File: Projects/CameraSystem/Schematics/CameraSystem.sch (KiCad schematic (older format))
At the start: 1 part, among them J1 USB_B_MICRO_SMD

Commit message: feat: set up layout
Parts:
- removed J1: USB_B_MICRO_SMD, MyLibraries:USB_B_MICRO_SMD, symbol USB_B_MICRO_SMD
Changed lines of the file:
@@
 EESchema Schematic File Version 2
+LIBS:cl-connectors
+LIBS:dk_Addressable-Specialty
+LIBS:dk_Alarms-Buzzers-and-Sirens
+LIBS:dk_Automotive-Relays
+LIBS:dk_Balun
+LIBS:dk_Barrel-Audio-Connectors
+LIBS:dk_Battery-Holders-Clips-Contacts
+LIBS:dk_Clock-Timing-Clock-Generators-PLLs-Frequency-Synthesizers
+LIBS:dk_Clock-Timing-Programmable-Timers-and-Oscillators
+LIBS:dk_Clock-Timing-Real-Time-Clocks
+LIBS:dk_Coaxial-Connectors-RF
+LIBS:dk_Current-Transducers
+LIBS:dk_Data-Acquisition-ADCs-DACs-Special-Purpose
+LIBS:dk_Data-Acquisition-Analog-to-Digital-Converters-ADC
+LIBS:dk_Data-Acquisition-Digital-Potentiometers
+LIBS:dk_Data-Acquisition-Digital-to-Analog-Converters-DAC
+LIBS:dk_Data-Acquisition-Touch-Screen-Controllers
+LIBS:dk_DC-DC-Converters
+LIBS:dk_Digital-Isolators
+LIBS:dk_Diodes-Bridge-Rectifiers
+LIBS:dk_Diodes-Rectifiers-Arrays
+LIBS:dk_Diodes-Rectifiers-Single
+LIBS:dk_Diodes-Zener-Single
+LIBS:dk_Display-Modules-LCD-OLED-Graphic
+LIBS:dk_Display-Modules-LED-Character-and-Numeric
+LIBS:dk_D-Sub-Connectors
+LIBS:dk_Embedded-Microcontrollers
+LIBS:dk_Encoders
+LIBS:dk_Evaluation-Boards-Sensors
+LIBS:dk_Ferrite-Beads-and-Chips
+LIBS:dk_Fixed-Inductors
+LIBS:dk_Fuses
+LIBS:dk_Gas-Sensors
+LIBS:dk_Humidity-Moisture-Sensors
+LIBS:dk_Image-Sensors-Camera
+LIBS:dk_Infrared-UV-Visible-Emitters
+LIBS:dk_Inrush-Current-Limiters-ICL
+LIBS:dk_Interface-Analog-Switches-Multiplexers-Demultiplexers
+LIBS:dk_Interface-Analog-Switches-Special-Purpose
+LIBS:dk_Interface-Controllers
+LIBS:dk_Interface-Drivers-Receivers-Transceivers
+LIBS:dk_Interface-I-O-Expanders
+LIBS:dk_Interface-Modules
+LIBS:dk_Interface-Sensor-and-Detector-Interfaces
+LIBS:dk_Interface-Sensor-Capacitive-Touch
+LIBS:dk_Interface-Specialized
+LIBS:dk_LED-Indication-Discrete
+LIBS:dk_LEDs-Circuit-Board-Indicators-Arrays-Light-Bars-Bar-Graphs
+LIBS:dk_Linear-Amplifiers-Audio
+LIBS:dk_Linear-Amplifiers-Instrumentation-OP-Amps-Buffer-Amps
+LIBS:dk_Linear-Comparators
+LIBS:dk_Logic-Buffers-Drivers-Receivers-Transceivers
+LIBS:dk_Logic-Flip-Flops
+LIBS:dk_Logic-Gates-and-Inverters
+LIBS:dk_Logic-Multivibrators
+LIBS:dk_Logic-Shift-Registers
+LIBS:dk_Logic-Signal-Switches-Multiplexers-Decoders
+LIBS:dk_Logic-Translators-Level-Shifters
+LIBS:dk_Magnetic-Sensors-Compass-Magnetic-Field-Modules
+LIBS:dk_Magnetic-Sensors-Linear-Compass-ICs
+LIBS:dk_Magnetic-Sensors-Switches-Solid-State
+LIBS:dk_Memory
+LIBS:dk_Memory-Connectors-PC-Card-Sockets
+LIBS:dk_Microphones
+LIBS:dk_Modular-Connectors-Jacks
+LIBS:dk_Modular-Connectors-Jacks-With-Magnetics
+LIBS:dk_Motion-Sensors-Accelerometers
+LIBS:dk_Motion-Sensors-IMUs-Inertial-Measurement-Units
+LIBS:dk_Motion-Sensors-Tilt-Switches
+LIBS:dk_Navigation-Switches-Joystick
+LIBS:dk_Optical-Sensors-Ambient-Light-IR-UV-Sensors
+LIBS:dk_Optical-Sensors-Photo-Detectors-Remote-Receiver
+LIBS:dk_Optical-Sensors-Photodiodes
+LIBS:dk_Optical-Sensors-Phototransistors
+LIBS:dk_Optical-Sensors-Reflective-Analog-Output
+LIBS:dk_Optoisolators-Logic-Output
+LIBS:dk_Optoisolators-Transistor-Photovoltaic-Output
+LIBS:dk_Optoisolators-Triac-SCR-Output
+LIBS:dk_Oscillators
+LIBS:dk_PMIC-AC-DC-Converters-Offline-Switchers
+LIBS:dk_PMIC-Battery-Chargers
+LIBS:dk_PMIC-Battery-Management
+LIBS:dk_PMIC-Current-Regulation-Management
+LIBS:dk_PMIC-Full-Half-Bridge-Drivers
+LIBS:dk_PMIC-Gate-Drivers
+LIBS:dk_PMIC-LED-Drivers
+LIBS:dk_PMIC-Motor-Drivers-Controllers
+LIBS:dk_PMIC-OR-Controllers-Ideal-Diodes
+LIBS:dk_PMIC-Power-Distribution-Switches-Load-Drivers
+LIBS:dk_PMIC-Power-Management-Specialized
+LIBS:dk_PMIC-RMS-to-DC-Converters
+LIBS:dk_PMIC-Supervisors
+LIBS:dk_PMIC-Thermal-Management
+LIBS:dk_PMIC-V-F-and-F-V-Converters
+LIBS:dk_PMIC-Voltage-Reference
+LIBS:dk_PMIC-Voltage-Regulators-DC-DC-Switching-Controllers
+LIBS:dk_PMIC-Voltage-Regulators-DC-DC-Switching-Regulators
+LIBS:dk_PMIC-Voltage-Regulators-Linear
+LIBS:dk_PMIC-Voltage-Regulators-Special-Purpose
+LIBS:dk_Power-Relays-Over-2-Amps
+LIBS:dk_Pressure-Sensors-Transducers
+LIBS:dk_Programmable-Oscillators
+LIBS:dk_Pushbutton-Switches
+LIBS:dk_Rectangular-Connectors-Headers-Male-Pins
+LIBS:dk_Reed-Relays
+LIBS:dk_Resistor-Networks-Arrays
+LIBS:dk_RF-Amplifiers
+LIBS:dk_RF-Antennas
+LIBS:dk_RF-Demodulators
+LIBS:dk_RF-Detectors
+LIBS:dk_RF-Evaluation-and-Development-Kits-Boards
+LIBS:dk_RFID-RF-Access-Monitoring-ICs
+LIBS:dk_RF-Receivers
+LIBS:dk_RF-Switches
+LIBS:dk_RF-Transceiver-ICs
+LIBS:dk_RF-Transceiver-Modules
+LIBS:dk_RF-Transmitters
+LIBS:dk_Rotary-Potentiometers-Rheostats
+LIBS:dk_Sensors-Transducers_Accessories
+LIBS:dk_Signal-Relays-Up-to-2-Amps
+LIBS:dk_Slide-Switches
+LIBS:dk_Solid-State-Relays
+LIBS:dk_Specialized-ICs
+LIBS:dk_Specialized-Sensors
+LIBS:dk_Surge-Suppression-ICs
+LIBS:dk_Tactile-Switches
+LIBS:dk_Temperature-Sensors-Analog-and-Digital-Output
+LIBS:dk_Thermal-Cutoffs-Thermal-Fuses
+LIBS:dk_Thyristors-DIACs-SIDACs
+LIBS:dk_Thyristors-SCRs
+LIBS:dk_Thyristors-TRIACs
+LIBS:dk_Toggle-Switches
+LIBS:dk_Transistors-Bipolar-BJT-Arrays
+LIBS:dk_Transistors-Bipolar-BJT-RF
+LIBS:dk_Transistors-Bipolar-BJT-Single
+LIBS:dk_Transistors-Bipolar-BJT-Single-Pre-Biased
+LIBS:dk_Transistors-FETs-MOSFETs-Arrays
+LIBS:dk_Transistors-FETs-MOSFETs-RF
+LIBS:dk_Transistors-FETs-MOSFETs-Single
+LIBS:dk_Transistors-JFETs
+LIBS:dk_Trimmer-Potentiometers
+LIBS:dk_TVS-Diodes
+LIBS:dk_TVS-Mixed-Technology
+LIBS:dk_USB-DVI-HDMI-Connectors
 LIBS:power
 LIBS:device
@@
 LIBS:contrib
 LIBS:valves
-LIBS:cl-connectors
+LIBS:cl-integrated_circuits
+LIBS:CameraSystem-cache
 EELAYER 25 0
 EELAYER END
 $Descr A4 11693 8268
 encoding utf-8
-Sheet 1 1
+Sheet 1 6
 Title ""
 Date ""
@@
 Comment4 ""
 $EndDescr
-$Comp
-L USB_B_MICRO_SMD J1
-U 1 1 5BB11F8A
-P 1250 1750
-F 0 "J1" H 1250 1450 60  0000 C CNN
-F 1 "USB_B_MICRO_SMD" H 1250 2100 60  0000 C CNN
-F 2 "MyLibraries:USB_B_MICRO_SMD" H 1250 1750 60  0001 C CNN
-F 3 "" H 1250 1750 60  0001 C CNN
-	1    1250 1750
-	-1   0    0    -1
-$EndComp
+$Sheet
+S 1000 1000 900  650
+U 5BB4C1AE
+F0 "Input_Interface" 60
+F1 "Input_Interface.sch" 60
+F2 "VDD_5V0" O R 1900 1150 60
+F3 "D-" B R 1900 1300 60
+F4 "D+" B R 1900 1450 60
+$EndSheet
+$Sheet
+S 2700 1700 1100 1050
+U 5BB4D99F
+F0 "Microcontroller" 60
+F1 "Microcontroller.sch" 60
+$EndSheet
+$Sheet
+S 4700 900  1100 750
+U 5BB4D9C1
+F0 "Wifi" 60
+F1 "Wifi.sch" 60
+$EndSheet
+$Sheet
+S 4650 2100 1000 800
+U 5BB4DA56
+F0 "Memory" 60
+F1 "Memory.sch" 60
+$EndSheet
+$Sheet
+S 6200 2150 850  800
+U 5BB4DA63
+F0 "Camera" 60
+F1 "Camera.sch" 60
+$EndSheet
 $EndSCHEMATC

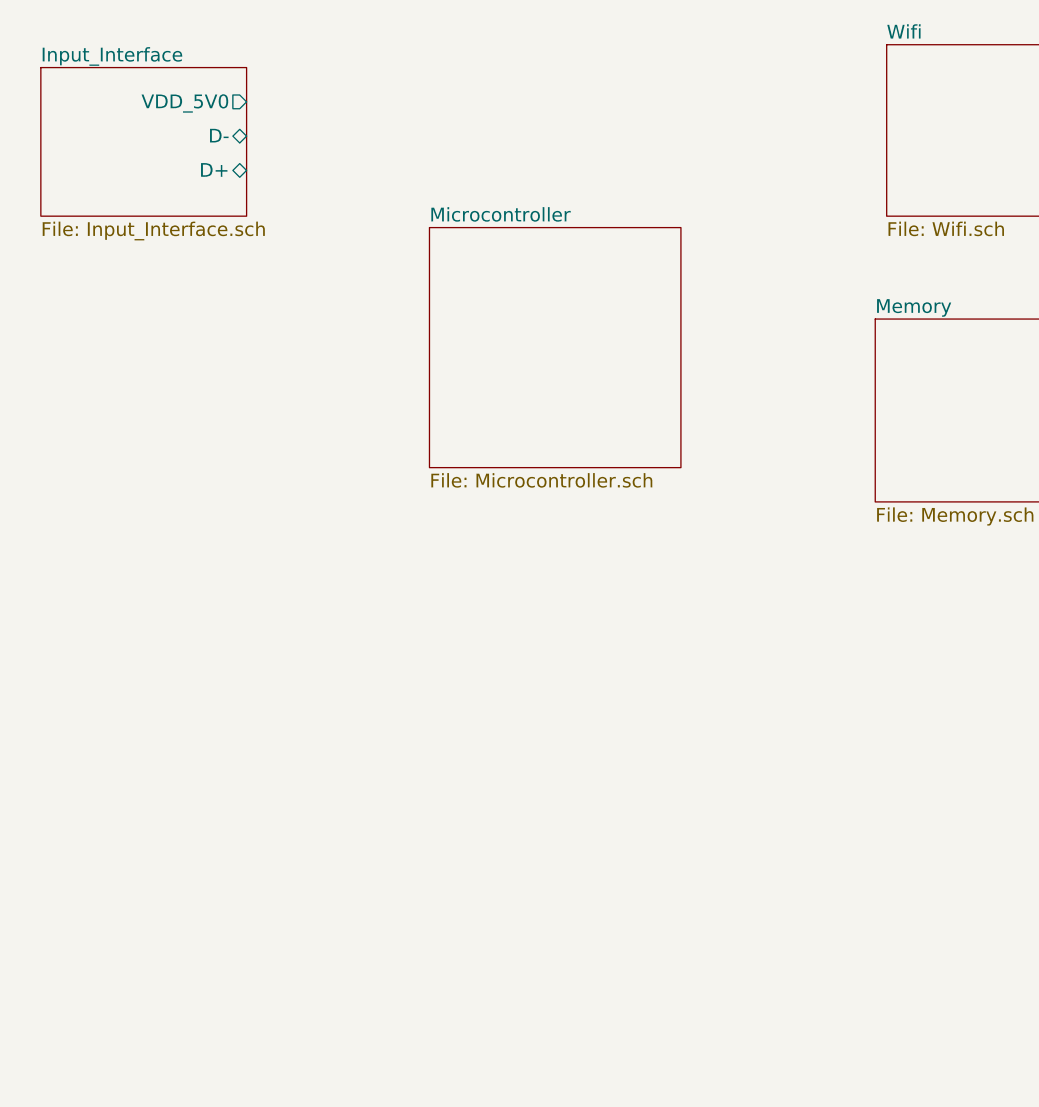
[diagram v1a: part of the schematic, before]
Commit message: feat:add led datasheets and microcontroler
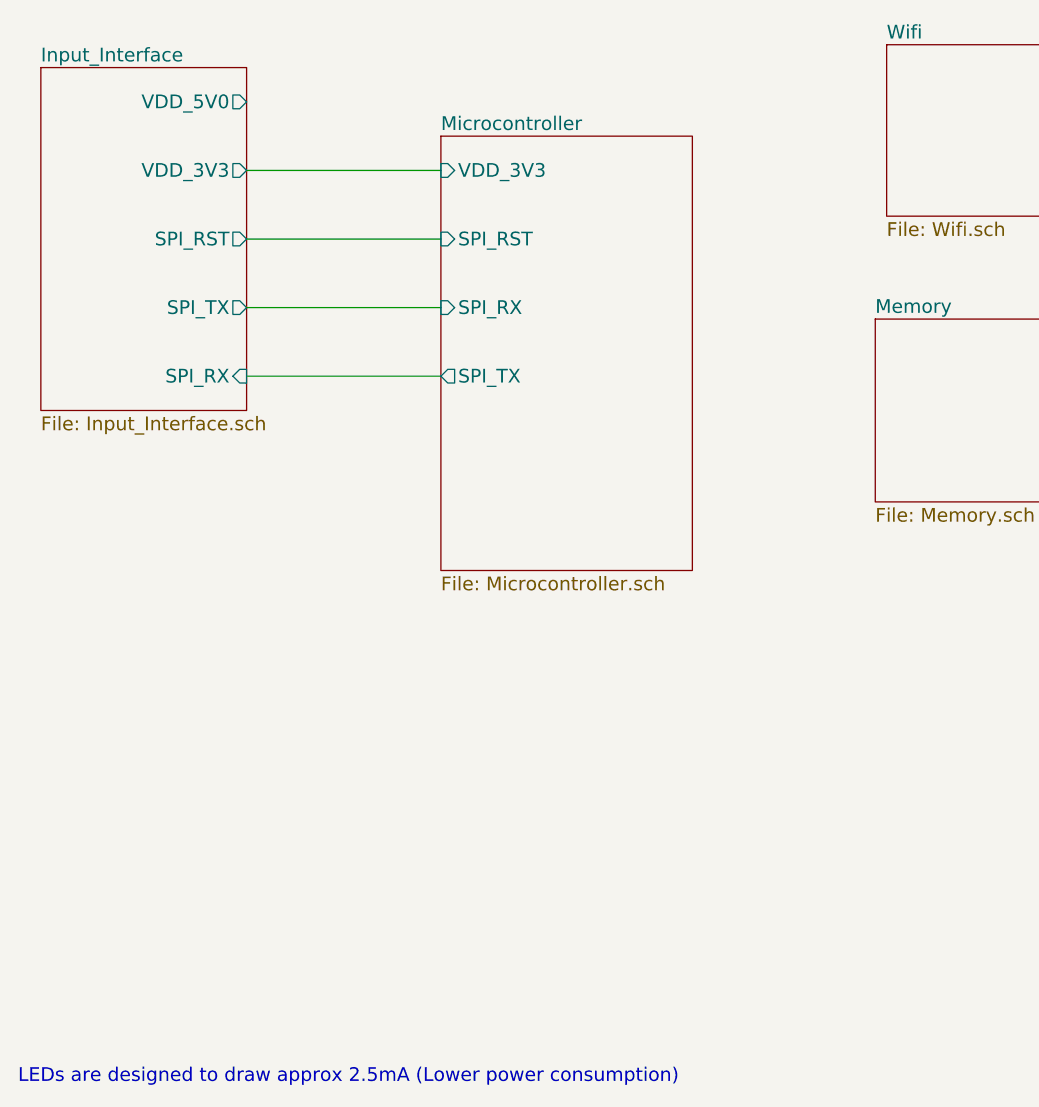
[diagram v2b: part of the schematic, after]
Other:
- note added: "LEDs are designed to draw approx 2.5mA (Lower power consumption)"
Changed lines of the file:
@@
 $EndDescr
 $Sheet
-S 1000 1000 900  650
+S 1000 1000 900  1500
 U 5BB4C1AE
 F0 "Input_Interface" 60
 F1 "Input_Interface.sch" 60
 F2 "VDD_5V0" O R 1900 1150 60
-F3 "D-" B R 1900 1300 60
-F4 "D+" B R 1900 1450 60
+F3 "VDD_3V3" O R 1900 1450 60
+F4 "SPI_RST" O R 1900 1750 60
+F5 "SPI_TX" O R 1900 2050 60
+F6 "SPI_RX" I R 1900 2350 60
 $EndSheet
 $Sheet
-S 2700 1700 1100 1050
+S 2750 1300 1100 1900
 U 5BB4D99F
 F0 "Microcontroller" 60
 F1 "Microcontroller.sch" 60
+F2 "VDD_3V3" I L 2750 1450 60
+F3 "SPI_RST" I L 2750 1750 60
+F4 "SPI_TX" O L 2750 2350 60
+F5 "SPI_RX" I L 2750 2050 60
 $EndSheet
 $Sheet
@@
 F1 "Camera.sch" 60
 $EndSheet
+Text Notes 900  5450 0    60   ~ 0
+LEDs are designed to draw approx 2.5mA (Lower power consumption)
+Wire Wire Line
+	2750 1450 1900 1450
+Wire Wire Line
+	1900 1750 2750 1750
+Wire Wire Line
+	1900 2050 2750 2050
+Wire Wire Line
+	1900 2350 2750 2350
 $EndSCHEMATC

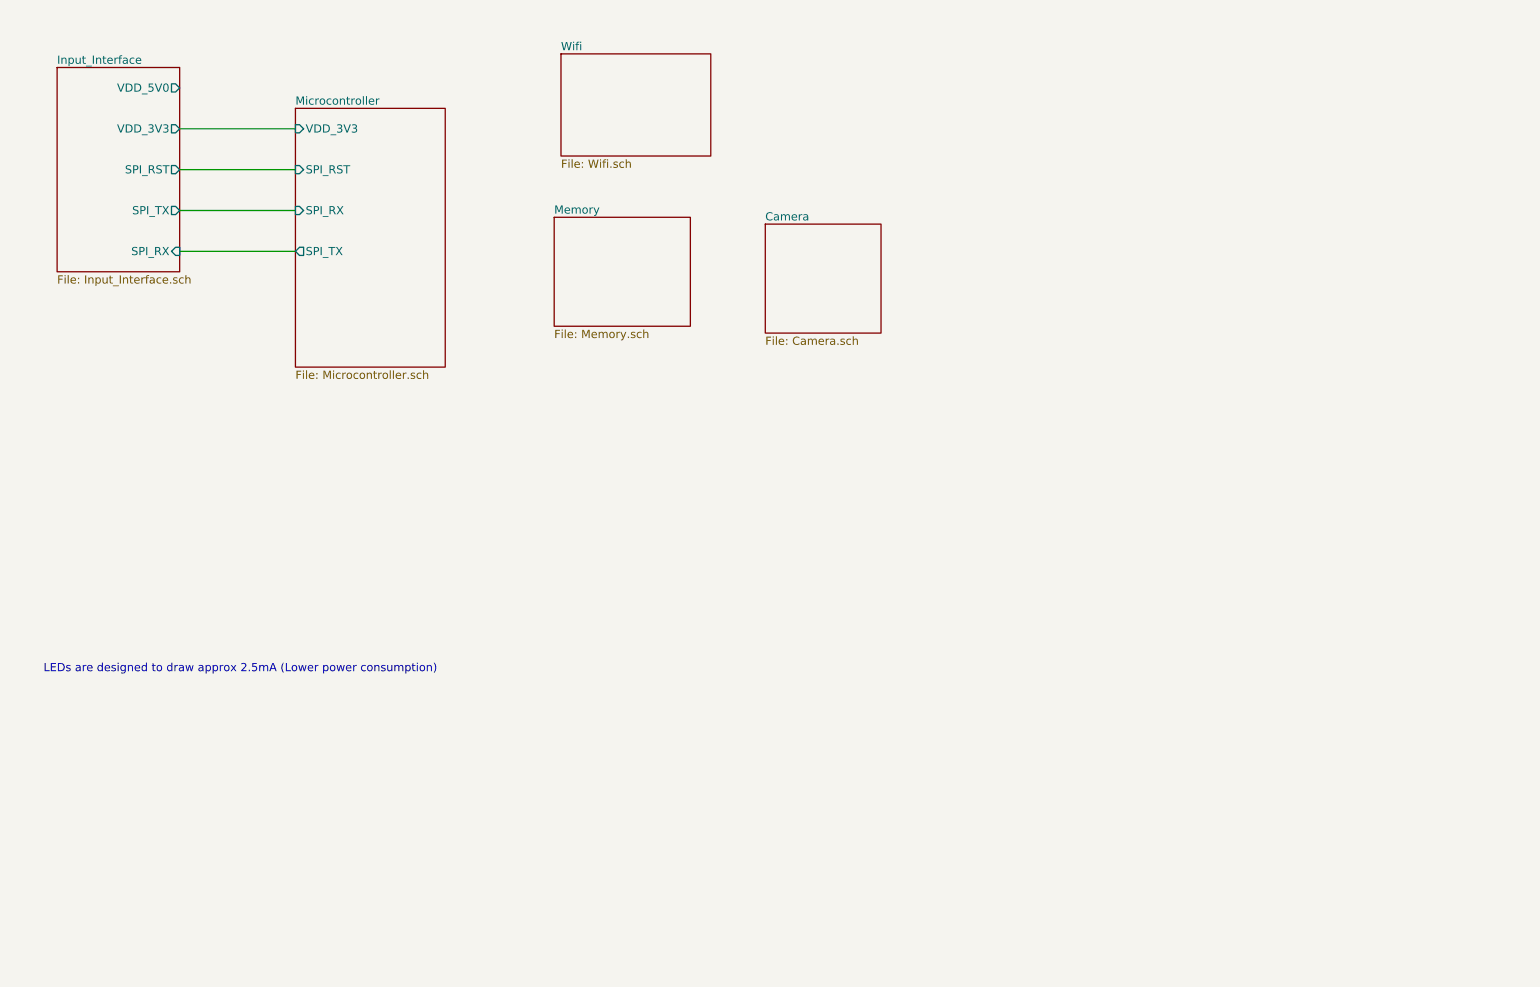
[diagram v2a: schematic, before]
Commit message: feat: add i2c ic, add additional datasheets and simulations
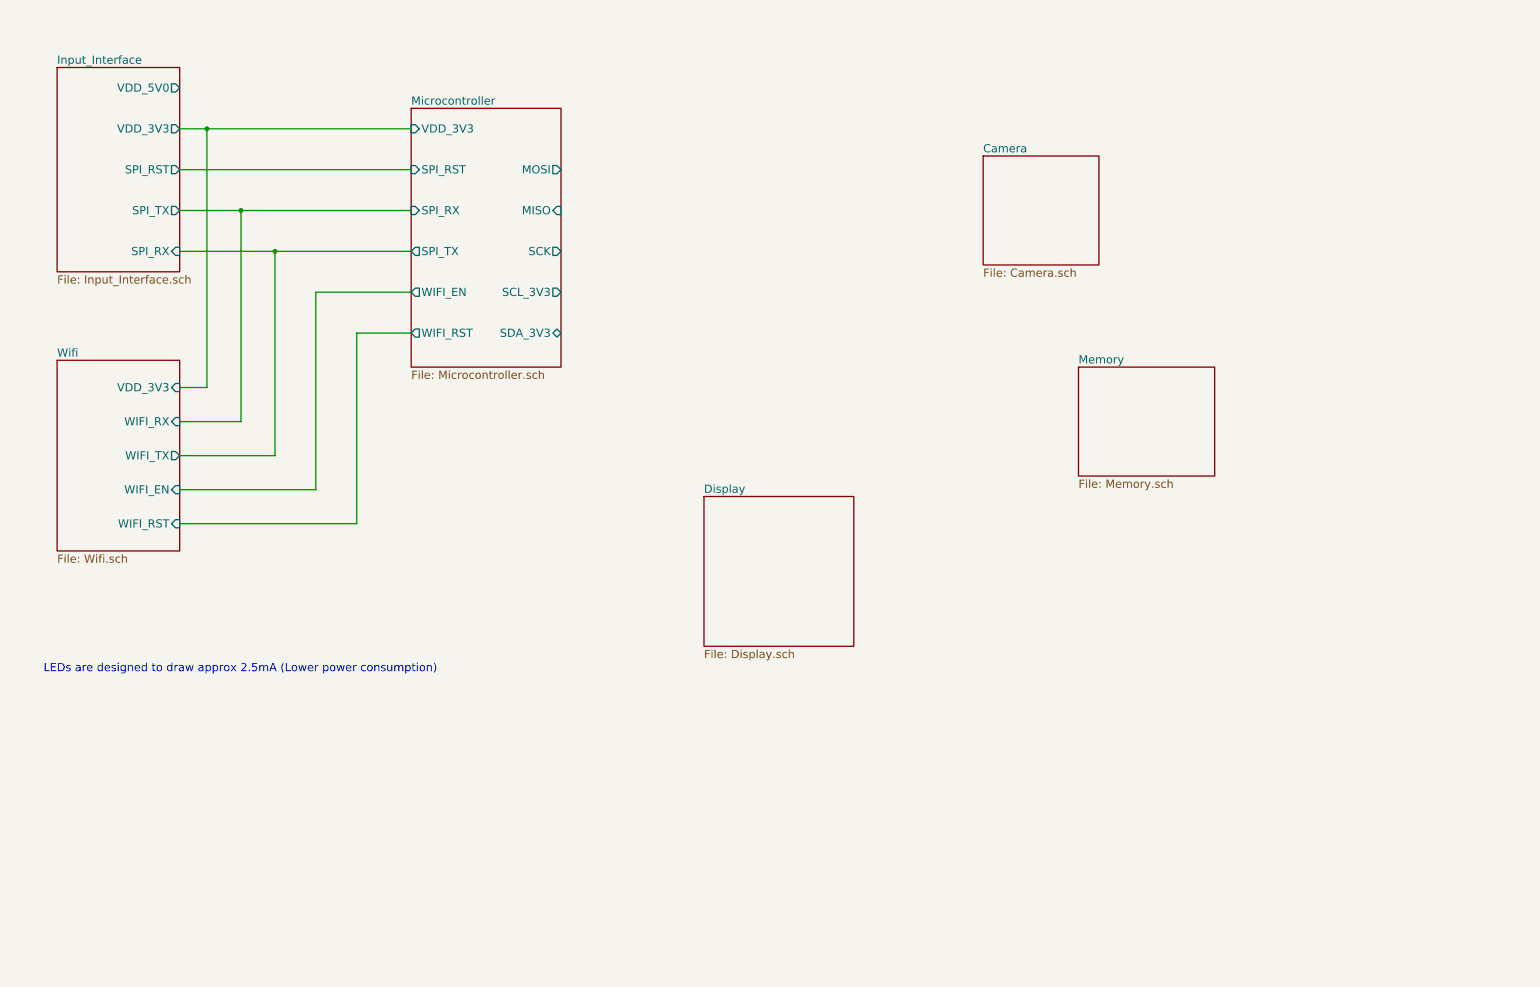
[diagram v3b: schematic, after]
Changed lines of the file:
@@
 $Descr A4 11693 8268
 encoding utf-8
-Sheet 1 6
+Sheet 1 7
 Title ""
 Date ""
@@
 $EndSheet
 $Sheet
-S 2750 1300 1100 1900
+S 3600 1300 1100 1900
 U 5BB4D99F
 F0 "Microcontroller" 60
 F1 "Microcontroller.sch" 60
-F2 "VDD_3V3" I L 2750 1450 60
-F3 "SPI_RST" I L 2750 1750 60
-F4 "SPI_TX" O L 2750 2350 60
-F5 "SPI_RX" I L 2750 2050 60
+F2 "VDD_3V3" I L 3600 1450 60
+F3 "SPI_RST" I L 3600 1750 60
+F4 "SPI_TX" O L 3600 2350 60
+F5 "SPI_RX" I L 3600 2050 60
+F6 "MOSI" O R 4700 1750 60
+F7 "MISO" I R 4700 2050 60
+F8 "SCK" O R 4700 2350 60
+F9 "WIFI_EN" O L 3600 2650 60
+F10 "WIFI_RST" O L 3600 2950 60
+F11 "SCL_3V3" O R 4700 2650 60
+F12 "SDA_3V3" B R 4700 2950 60
 $EndSheet
 $Sheet
-S 4700 900  1100 750
+S 1000 3150 900  1400
 U 5BB4D9C1
 F0 "Wifi" 60
 F1 "Wifi.sch" 60
+F2 "VDD_3V3" I R 1900 3350 60
+F3 "WIFI_TX" O R 1900 3850 60
+F4 "WIFI_RX" I R 1900 3600 60
+F5 "WIFI_RST" I R 1900 4350 60
+F6 "WIFI_EN" I R 1900 4100 60
 $EndSheet
 $Sheet
-S 4650 2100 1000 800
+S 8500 3200 1000 800
 U 5BB4DA56
 F0 "Memory" 60
@@
 $EndSheet
 $Sheet
-S 6200 2150 850  800
+S 7800 1650 850  800
 U 5BB4DA63
 F0 "Camera" 60
@@
 LEDs are designed to draw approx 2.5mA (Lower power consumption)
 Wire Wire Line
-	2750 1450 1900 1450
+	3600 1450 1900 1450
 Wire Wire Line
-	1900 1750 2750 1750
+	1900 1750 3600 1750
 Wire Wire Line
-	1900 2050 2750 2050
+	1900 2050 3600 2050
 Wire Wire Line
-	1900 2350 2750 2350
+	1900 2350 3600 2350
+Wire Wire Line
+	1900 3350 2100 3350
+Wire Wire Line
+	2100 3350 2100 1450
+Connection ~ 2100 1450
+Wire Wire Line
+	1900 3600 2350 3600
+Wire Wire Line
+	2350 3600 2350 2050
+Connection ~ 2350 2050
+Wire Wire Line
+	1900 3850 2600 3850
+Wire Wire Line
+	2600 3850 2600 2350
+Connection ~ 2600 2350
+Wire Wire Line
+	1900 4100 2900 4100
+Wire Wire Line
+	2900 4100 2900 2650
+Wire Wire Line
+	2900 2650 3600 2650
+Wire Wire Line
+	1900 4350 3200 4350
+Wire Wire Line
+	3200 4350 3200 2950
+Wire Wire Line
+	3200 2950 3600 2950
+$Sheet
+S 5750 4150 1100 1100
+U 5BB9CC6E
+F0 "Display" 60
+F1 "Display.sch" 60
+$EndSheet
 $EndSCHEMATC
